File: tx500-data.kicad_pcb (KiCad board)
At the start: 2 copper layers, 50 x 79 mm, 69 parts, among them J1 USB_C_Receptacle, J2 FTDI, J3 AUDIO, SW1 VCCIO, U1 TUSB2036, U2 FT232RL, U3 HS-100B, U4 TPS76333, U5 SN75240, U6 TPS2041, Y1 AWSCR-6.00CPLA

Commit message: Fix up fabrication files
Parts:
- L1, L2: footprint Inductor_SMD:L_0603_1608Metric -> Inductor_SMD:L_0805_2012Metric
- moved L1 1.00 mm to (134.0, 67.0)
- moved L2 1.00 mm to (145.0, 64.0)
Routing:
- net VBUS: track 24.0 -> 23.3 mm
- net Net-(J1-PadA4): track 32.0 -> 32.8 mm

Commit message: Add BOM
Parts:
- R12, R13, R6, R7, R8, R9: value 27 -> 27R
- R18, R20, R21: value 330 -> 330R

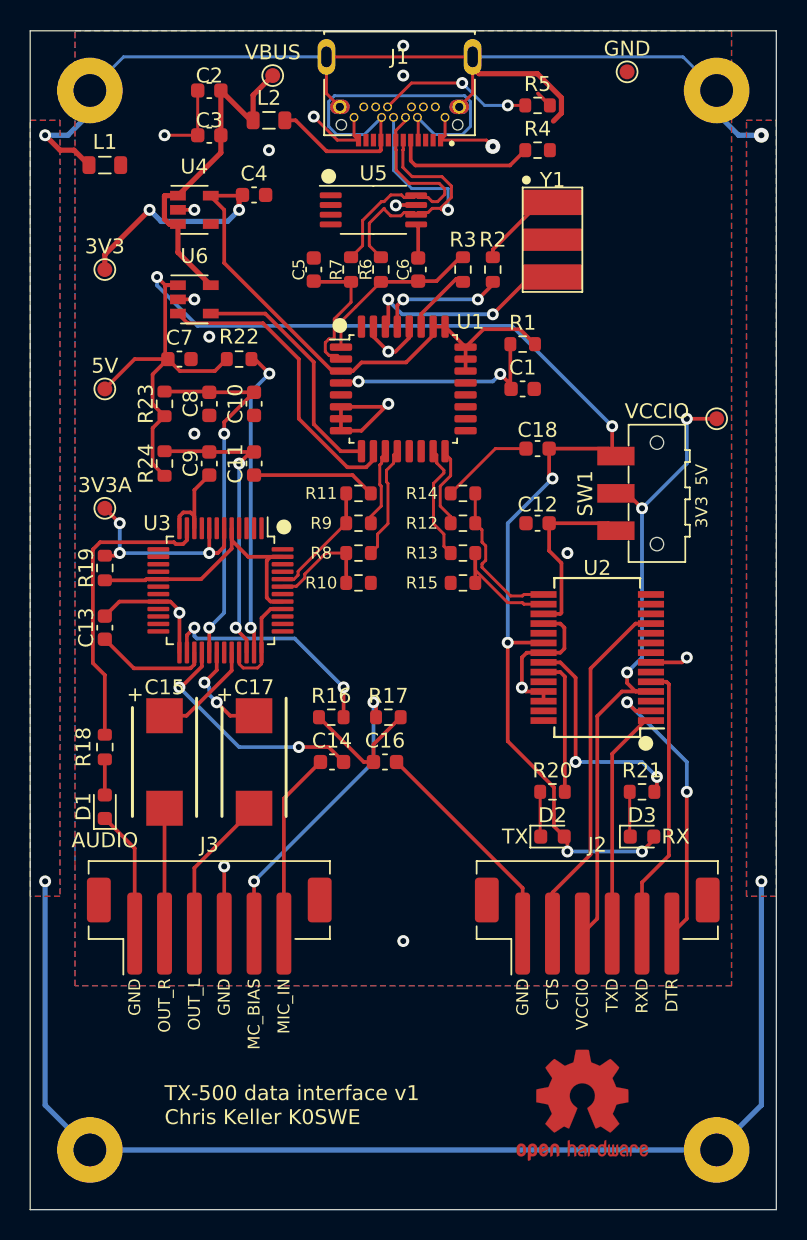
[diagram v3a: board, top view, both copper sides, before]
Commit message: Fix USB-C footprint
During fabrication review, the production engineer noticed that the 5V trace intersected with the shield pads. This was because they were using F.CU and B.CU graphics which weren't getting included in the pad margins.
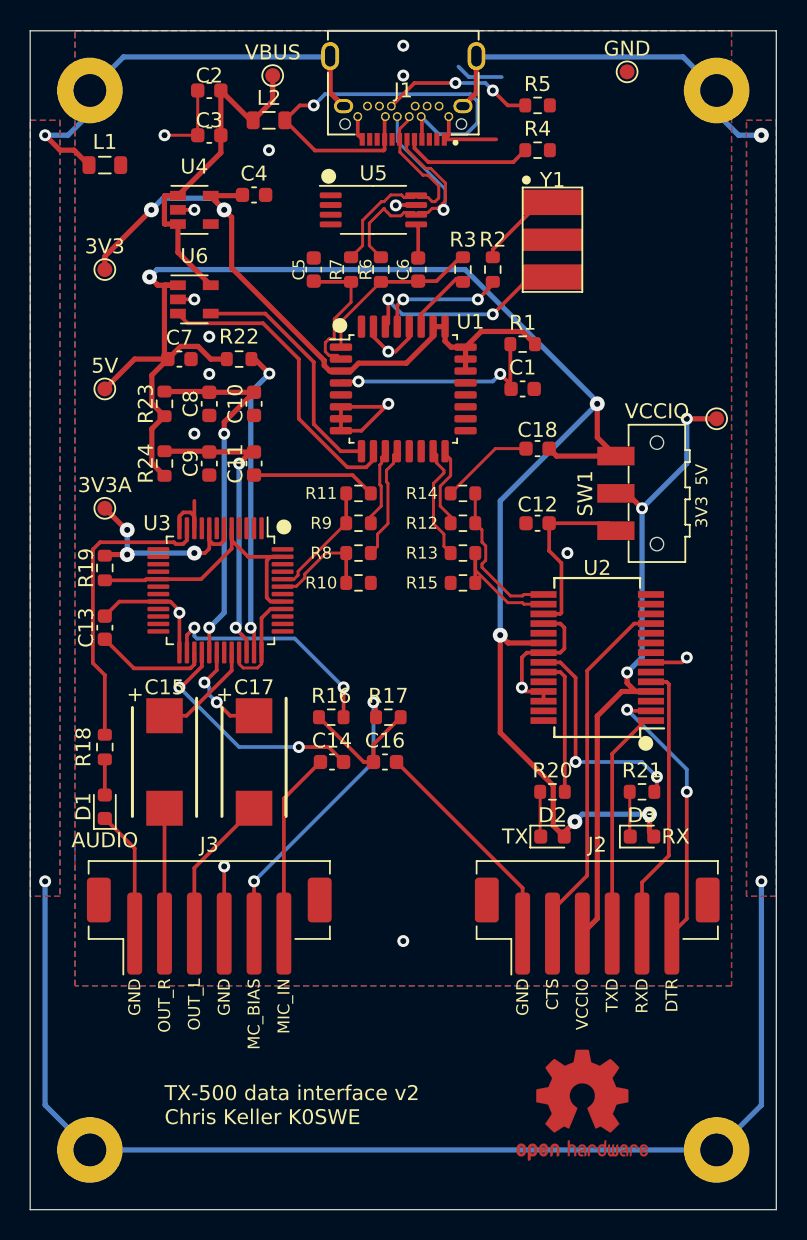
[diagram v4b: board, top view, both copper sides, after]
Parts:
- moved J1 1.77 mm to (154.0, 58.0), turned to 0 degrees
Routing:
- net GND1: track 157.8 -> 139.7 mm
- net +5V: track 106.9 -> 114.5 mm, vias 6 -> 5
- net GNDREF: track 114.2 -> 110.3 mm, vias 19 -> 18
- net /DR+: track 25.4 -> 22.3 mm
- net +3V3: track 48.5 -> 46.9 mm
- net Net-(J1-PadA4): track 32.8 -> 31.2 mm, vias 0 -> 1
- net /DR-: track 17.5 -> 16.0 mm
- net Net-(J1-PadA5): track 9.62 -> 8.74 mm
- net /3V3A: track 14.6 -> 15.3 mm
- net /DTR: track 19.4 -> 18.7 mm
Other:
- net class Default: clearance 0.2 -> 0.15
- net class Power: clearance 0.2 -> 0.15
- net class USB-C removed
- rule trace_clearance: 0.2 -> 0.15
- board text added: "TX-500 data interface v2 Chris Keller K0SWE"
- board text removed: "TX-500 data interface v1 Chris Keller K0SWE"

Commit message: Add bulkhead parts to schematic
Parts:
- J2: value FTDI -> CAT
